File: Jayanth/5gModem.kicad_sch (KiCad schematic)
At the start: 36 parts, among them J4 SIM_Card_Shielded, J5 RJ45_JK0654219, U4 RG520N, U6 KSZ9031RNXCA, Y3 25Mhz Crystal

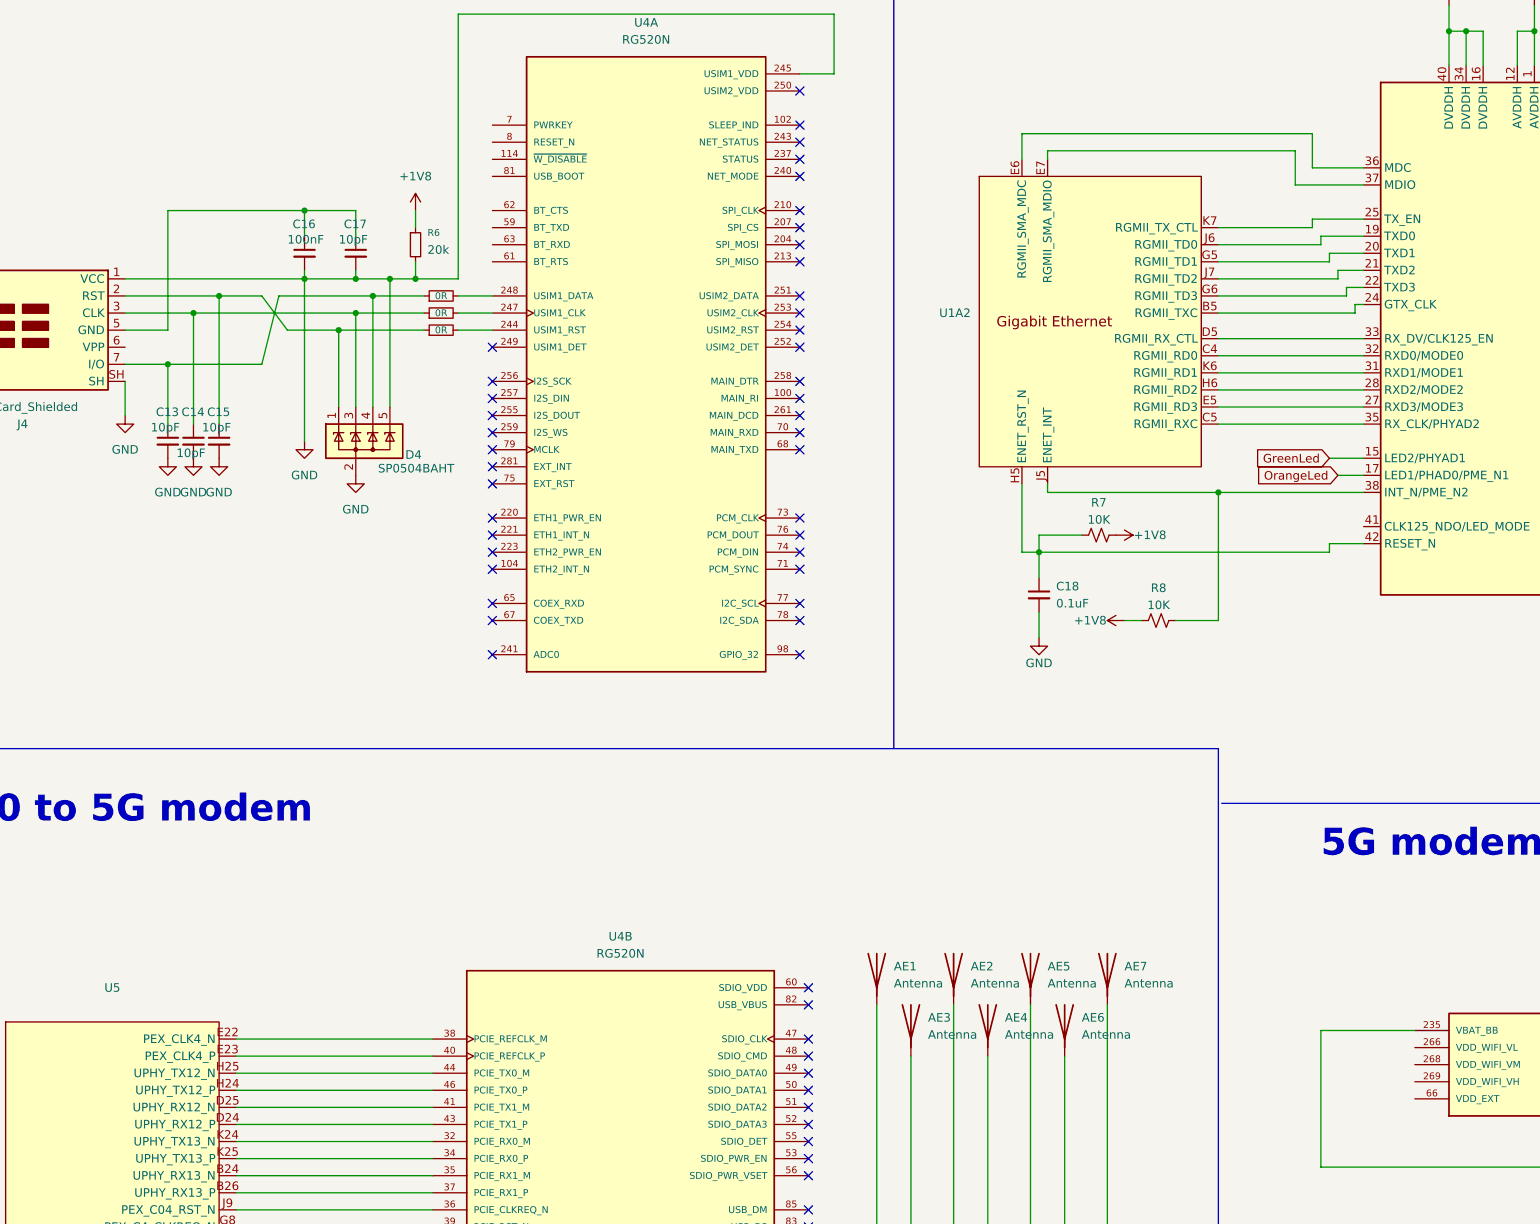
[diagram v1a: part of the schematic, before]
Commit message: added fan ctrl
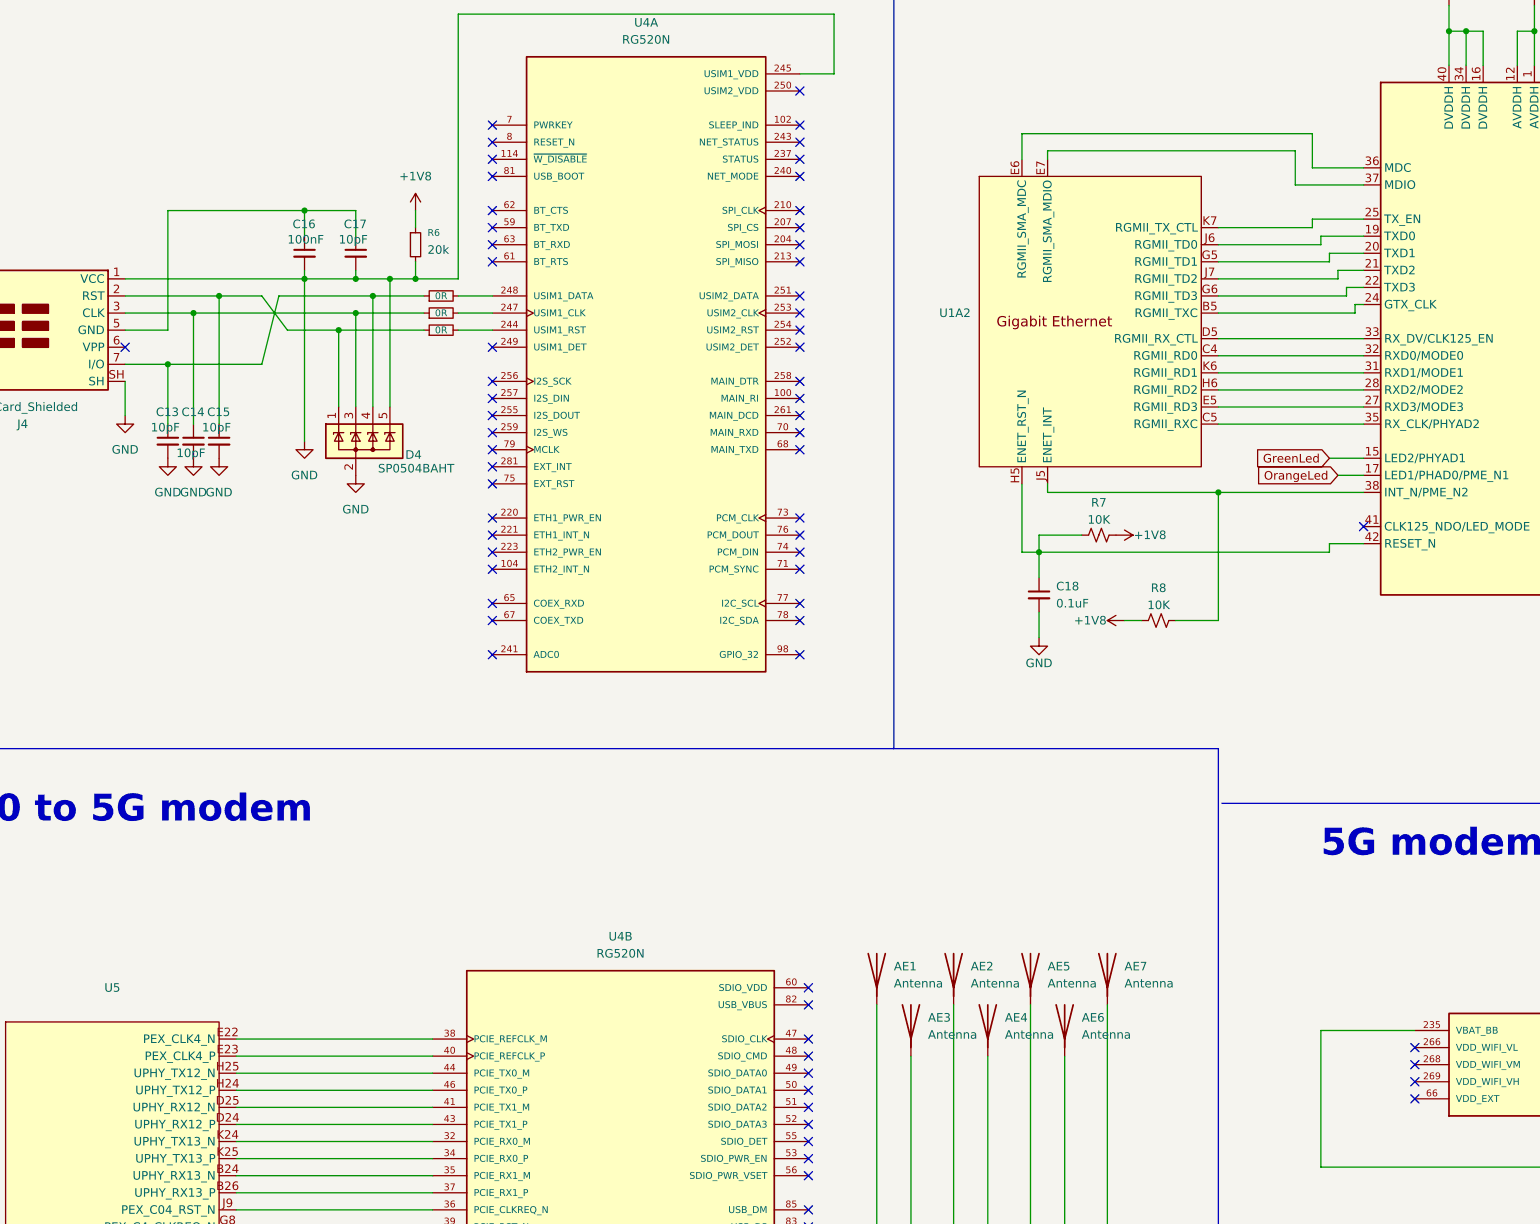
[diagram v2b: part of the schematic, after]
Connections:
- no-connect marks 75 -> 89
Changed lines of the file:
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@@
+	)
+	(no_connect
+		(at 104.14 67.31)
 	)
 	(no_connect
@@
 	)
 	(no_connect
+		(at 49.53 87.63)
+	)
+	(no_connect
 		(at 151.13 185.42)
 	)
@@
 	)
 	(no_connect
+		(at 233.68 114.3)
+	)
+	(no_connect
 		(at 95.25 243.84)
 	)
@@
 	)
 	(no_connect
+		(at 104.14 59.69)
+	)
+	(no_connect
+		(at 104.14 72.39)
+	)
+	(no_connect
 		(at 104.14 105.41)
 	)
@@
 	)
 	(no_connect
+		(at 104.14 57.15)
+	)
+	(no_connect
 		(at 151.13 233.68)
 	)
@@
 	)
 	(no_connect
+		(at 241.3 194.31)
+	)
+	(no_connect
 		(at 151.13 200.66)
 	)
@@
 	)
 	(no_connect
+		(at 104.14 74.93)
+	)
+	(no_connect
 		(at 151.13 195.58)
 	)
@@
 	)
 	(no_connect
+		(at 104.14 54.61)
+	)
+	(no_connect
 		(at 149.86 102.87)
 	)
@@
 	)
 	(no_connect
+		(at 104.14 69.85)
+	)
+	(no_connect
 		(at 151.13 261.62)
 	)
@@
 	)
 	(no_connect
+		(at 241.3 196.85)
+	)
+	(no_connect
 		(at 149.86 100.33)
 	)
@@
 	)
 	(no_connect
+		(at 104.14 62.23)
+	)
+	(no_connect
 		(at 149.86 54.61)
 	)
@@
 	)
 	(no_connect
+		(at 241.3 199.39)
+	)
+	(no_connect
 		(at 149.86 120.65)
 	)
@@
 		(at 151.13 218.44)
 	)
+	(no_connect
+		(at 241.3 191.77)
+	)
 	(wire
